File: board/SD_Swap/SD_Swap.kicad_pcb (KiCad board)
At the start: 4 copper layers, 32 x 27 mm, 44 parts, among them J1 USB_C, Q1 Q_Dual_PNP_PNP_E1B1C2E2B2C1, U1 74LVC2G14, U2 RTS5306E, U3 PCB_SD, U4 93AAxxAT, U5 TS3A27518ERTW, U6 SD_SOCKET, U7 AZ1117-3.3, Y1 12MHz

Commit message: tmp
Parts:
- J1: footprint Connector_USB:USB_C_Receptacle_Amphenol_12401548E4-2A -> USB-C:USB_C_Receptacle_Amphenol_10137061-00021LF
- moved J1 5.65 mm to (99.4, 77.9)

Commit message: tmp fix for my mistake
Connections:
- J1 pad A10: /SS_RX- -> unconnected-(J1-RX2--PadA10)
- J1 pad A11: /SS_RX+ -> unconnected-(J1-RX2+-PadA11)
- J1 pad B2: /SS_TX+ -> unconnected-(J1-TX2+-PadB2)
- J1 pad B3: /SS_TX- -> unconnected-(J1-TX2--PadB3)
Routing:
- net /SS_RX+: track 21.2 -> 9.65 mm, vias 2 -> 1
- net /SS_RX-: track 21.1 -> 9.57 mm, vias 2 -> 1
- net /SS_TX+: track 10.3 -> 1.73 mm, vias 1 -> 0
- net /SS_TX-: track 10.2 -> 1.73 mm, vias 1 -> 0

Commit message: tmp
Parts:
- moved C7 1.54 mm to (105.0, 80.6)
- moved C9 0.84 mm to (103.2, 80.7)
- moved R11 0.84 mm to (104.0, 80.7)
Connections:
- D2 pad 2: VCC -> GND
- D2 pad 3: GND -> Net-(D2-A1)
- D2 pad 4: Net-(D2-A1) -> VCC
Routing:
- net +3.3V: track 28.8 -> 26.0 mm, vias 6 -> 5
- net /USB-: track 17.8 -> 15.9 mm
- net /USB+: track 19.0 -> 17.3 mm
- net Net-(U2-REFF): track 2.32 -> 0.80 mm
- net +5V: track 12.5 -> 11.1 mm
- net +1V2: track 23.4 -> 22.7 mm

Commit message: tmp
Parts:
- moved C3 2.48 mm to (116.7, 77.5), turned to 135 degrees
- moved JP3 1.90 mm to (100.3, 93.3)
- moved C2 1.76 mm to (115.7, 78.4), turned to 135 degrees
- moved C7 1.11 mm to (105.5, 81.6), turned to 0 degrees
- moved U5 0.90 mm to (118.9, 81.5)
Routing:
- net +3.3V: track 26.0 -> 32.9 mm
- net Net-(U2-SD_D1): track 13.5 -> 7.67 mm
- net Net-(U5-COM2): track 15.9 -> 10.1 mm
- net /SD_SEL: track 33.7 -> 30.0 mm, vias 2 -> 3
- net Net-(U2-SD_D0): track 12.8 -> 9.40 mm
- net Net-(U5-COM3): track 14.0 -> 10.9 mm
- net Net-(U3-DAT3): track 17.6 -> 15.0 mm
- net Net-(U3-CLK): track 17.6 -> 15.2 mm
- net GND: track 5.56 -> 3.31 mm, vias 87 -> 80
- net Net-(U3-CMD): track 17.6 -> 15.4 mm
- net Net-(U5-COM1): track 13.5 -> 11.4 mm
- net Net-(U2-REFF): track 0.80 -> 2.72 mm
- net Net-(U3-DAT2): track 17.7 -> 15.9 mm
- net Net-(U2-SD_CLK): track 12.9 -> 11.1 mm
- net Net-(U5-COM6): track 14.0 -> 12.5 mm
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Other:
- board text added: "USB3 and 2 are 90ohm diff pair"
- board text added: "{dblquote}(1) Driver Type B Type B driver is the default drive strength, targeted for a fixed impedance distributed system with 50 ohm transmission line, at all available frequencies. Therefore, it is defined as 50 ohm nominal driver. This driver can support total CL of about 15pF for UHS104 card and about 30pF for UHS50 card. Drive strength B is the reference driver for definitions of all the re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"
- board text removed: "UHS50 cards must have 50ohm nominal impedance. There is no length matich requirements but so 0.5mm is ok."

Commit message: tmp
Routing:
- net GND: track 3.31 -> 6.04 mm, vias 80 -> 88
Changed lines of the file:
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@@
     )
     (pad_to_mask_clearance 0.038)
+    (grid_origin 137.7 68.9)
     (pcbplotparams
       (layerselection 0x00000fc_ffffffff)
@@
     (effects (font (size 1 1) (thickness 0.15)) (justify left))
   )
+  (segment (start 119.95 81.15) (end 119.95 81.15) (width 0.25) (layer "F.Cu") (net 1))
+  (segment (start 120.45 81.4) (end 120.2 81.4) (width 0.25) (layer "F.Cu") (net 1))
+  (segment (start 119.95 80.9) (end 119.7 80.9) (width 0.25) (layer "F.Cu") (net 1))
   (segment (start 103.65 92.05) (end 102.625 92.05) (width 0.2) (layer "F.Cu") (net 1))
   (segment (start 102.625 92.05) (end 102.6 92.025) (width 0.2) (layer "F.Cu") (net 1))
-  (segment (start 120.800699 82.313173) (end 119.961009 81.473483) (width 0.25) (layer "F.Cu") (net 1))
-  (segment (start 119.961009 81.473483) (end 118.900349 81.473483) (width 0.25) (layer "F.Cu") (net 1))
+  (segment (start 118.95 81.4) (end 118.900349 81.473483) (width 0.25) (layer "F.Cu") (net 1))
+  (segment (start 119.7 80.9) (end 119.7 80.9) (width 0.25) (layer "F.Cu") (net 1))
+  (segment (start 120.800699 82.313173) (end 120.45 81.962474) (width 0.25) (layer "F.Cu") (net 1))
+  (segment (start 120.2 81.712474) (end 120.45 81.4) (width 0.25) (layer "F.Cu") (net 1))
+  (segment (start 120.2 81.4) (end 119.95 81.4) (width 0.25) (layer "F.Cu") (net 1))
+  (segment (start 119.961009 81.473483) (end 119.95 81.15) (width 0.25) (layer "F.Cu") (net 1))
+  (segment (start 119.95 81.4) (end 119.887526 81.4) (width 0.25) (layer "F.Cu") (net 1))
+  (segment (start 119.887526 81.4) (end 119.961009 81.473483) (width 0.25) (layer "F.Cu") (net 1))
+  (segment (start 120.45 81.962474) (end 120.45 81.65) (width 0.25) (layer "F.Cu") (net 1))
+  (segment (start 119.7 80.9) (end 119.45 80.9) (width 0.25) (layer "F.Cu") (net 1))
+  (segment (start 119.95 81.15) (end 119.95 80.9) (width 0.25) (layer "F.Cu") (net 1))
+  (segment (start 119.95 81.9) (end 120.2 81.712474) (width 0.25) (layer "F.Cu") (net 1))
+  (segment (start 119.45 81.4) (end 118.95 81.4) (width 0.25) (layer "F.Cu") (net 1))
+  (segment (start 120.137526 81.65) (end 119.95 81.9) (width 0.25) (layer "F.Cu") (net 1))
+  (segment (start 119.45 80.9) (end 119.45 81.4) (width 0.25) (layer "F.Cu") (net 1))
+  (segment (start 120.45 81.65) (end 120.137526 81.65) (width 0.25) (layer "F.Cu") (net 1))
   (via (at 93 71) (size 0.6) (drill 0.3) (layers "F.Cu" "B.Cu") (free) (net 1))
+  (via (at 119.95 80.9) (size 0.4) (drill 0.2) (layers "F.Cu" "B.Cu") (net 1))
   (via (at 116 90) (size 0.6) (drill 0.3) (layers "F.Cu" "B.Cu") (free) (net 1))
   (via (at 109 79) (size 0.4) (drill 0.2) (layers "F.Cu" "B.Cu") (net 1))
@@
   (via (at 108.5 77) (size 0.4) (drill 0.2) (layers "F.Cu" "B.Cu") (net 1))
   (via (at 109.5 78.5) (size 0.4) (drill 0.2) (layers "F.Cu" "B.Cu") (net 1))
+  (via (at 118.45 80.4) (size 0.4) (drill 0.2) (layers "F.Cu" "B.Cu") (net 1))
   (via (at 108 78.5) (size 0.4) (drill 0.2) (layers "F.Cu" "B.Cu") (net 1))
   (via (at 108 79.5) (size 0.4) (drill 0.2) (layers "F.Cu" "B.Cu") (net 1))
@@
   (via (at 131 86) (size 0.6) (drill 0.3) (layers "F.Cu" "B.Cu") (free) (net 1))
   (via (at 109 79.5) (size 0.4) (drill 0.2) (layers "F.Cu" "B.Cu") (net 1))
+  (via (at 118.95 80.9) (size 0.4) (drill 0.2) (layers "F.Cu" "B.Cu") (net 1))
   (via (at 109 77) (size 0.4) (drill 0.2) (layers "F.Cu" "B.Cu") (net 1))
   (via (at 107.5 79.5) (size 0.4) (drill 0.2) (layers "F.Cu" "B.Cu") (net 1))
@@
   (via (at 94 93) (size 0.6) (drill 0.3) (layers "F.Cu" "B.Cu") (free) (net 1))
   (via (at 109.5 79.5) (size 0.4) (drill 0.2) (layers "F.Cu" "B.Cu") (net 1))
+  (via (at 119.95 81.9) (size 0.4) (drill 0.2) (layers "F.Cu" "B.Cu") (net 1))
   (via (at 115 71) (size 0.6) (drill 0.3) (layers "F.Cu" "B.Cu") (free) (net 1))
   (via (at 120 86) (size 0.6) (drill 0.3) (layers "F.Cu" "B.Cu") (free) (net 1))
@@
   (via (at 94 70) (size 0.6) (drill 0.3) (layers "F.Cu" "B.Cu") (free) (net 1))
   (via (at 107.5 78.5) (size 0.4) (drill 0.2) (layers "F.Cu" "B.Cu") (net 1))
+  (via (at 119.45 81.4) (size 0.4) (drill 0.2) (layers "F.Cu" "B.Cu") (net 1))
   (via (at 96 94) (size 0.6) (drill 0.3) (layers "F.Cu" "B.Cu") (free) (net 1))
   (via (at 107 78) (size 0.4) (drill 0.2) (layers "F.Cu" "B.Cu") (net 1))
   (via (at 109.6 94) (size 0.6) (drill 0.3) (layers "F.Cu" "B.Cu") (free) (net 1))
+  (via (at 120.45 81.4) (size 0.4) (drill 0.2) (layers "F.Cu" "B.Cu") (net 1))
+  (via (at 119.45 80.4) (size 0.4) (drill 0.2) (layers "F.Cu" "B.Cu") (net 1))
   (via (at 108.5 79) (size 0.4) (drill 0.2) (layers "F.Cu" "B.Cu") (net 1))
   (via (at 108 77) (size 0.4) (drill 0.2) (layers "F.Cu" "B.Cu") (net 1))
@@
   (via (at 109.5 78) (size 0.4) (drill 0.2) (layers "F.Cu" "B.Cu") (net 1))
   (via (at 110 77) (size 0.4) (drill 0.2) (layers "F.Cu" "B.Cu") (net 1))
+  (via (at 118.95 79.9) (size 0.4) (drill 0.2) (layers "F.Cu" "B.Cu") (net 1))
   (via (at 110 79) (size 0.4) (drill 0.2) (layers "F.Cu" "B.Cu") (net 1))
   (via (at 108.5 78.5) (size 0.4) (drill 0.2) (layers "F.Cu" "B.Cu") (net 1))
@@
   (via (at 114.2 86.4) (size 0.4) (drill 0.2) (layers "F.Cu" "B.Cu") (net 48))
   (via (at 118.096015 78.671573) (size 0.4) (drill 0.2) (layers "F.Cu" "B.Cu") (net 48))
-  (segment (start 118.096015 78.671573) (end 118.096015 83.303985) (width 0.22) (layer "In1.Cu") (net 48))
+  (segment (start 117.85 78.917588) (end 118.096015 78.671573) (width 0.22) (layer "In1.Cu") (net 48))
+  (segment (start 117.85 83.55) (end 115 86.4) (width 0.22) (layer "In1.Cu") (net 48))
   (segment (start 115 86.4) (end 114.2 86.4) (width 0.22) (layer "In1.Cu") (net 48))
-  (segment (start 118.096015 83.303985) (end 115 86.4) (width 0.22) (layer "In1.Cu") (net 48))
+  (segment (start 117.85 83.55) (end 117.85 78.917588) (width 0.22) (layer "In1.Cu") (net 48))
   (segment (start 114.15 87.311715) (end 114.15 86.45) (width 0.22) (layer "B.Cu") (net 48))
   (segment (start 114.15 86.45) (end 114.2 86.4) (width 0.22) (layer "B.Cu") (net 48))
@@
   )
   (zone (net 3) (net_name "+3.3V") (layer "In1.Cu") (hatch edge 0.508)
-    (connect_pads (clearance 0.2))
+    (connect_pads (clearance 0.3))
     (min_thickness 0.15) (filled_areas_thickness no)
     (fill yes (thermal_gap 0.1) (thermal_bridge_width 0.2))
@@
   )
   (zone (net 10) (net_name "/SD_VCC") (layer "In2.Cu") (hatch edge 0.508)
-    (connect_pads (clearance 0.2))
+    (connect_pads (clearance 0.3))
     (min_thickness 0.15) (filled_areas_thickness no)
     (fill yes (thermal_gap 0.1) (thermal_bridge_width 0.2))

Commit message: final?
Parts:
- moved C5 1.67 mm to (111.7, 82.6)
- moved C4 1.59 mm to (111.7, 81.8)
- moved U7 0.60 mm to (106.6, 85.7)
- moved C1 0.35 mm to (113.8, 91.7)
- moved Q1 0.35 mm to (111.6, 91.3)
- moved R5 0.25 mm to (105.3, 90.2)
- moved R7 0.25 mm to (107.1, 90.2)
- moved R8 0.10 mm to (111.3, 93.7)
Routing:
- net /USB+: track 17.3 -> 15.9 mm
- net /USB-: track 15.9 -> 14.7 mm
- net +3.3V: track 32.9 -> 33.7 mm
- net Net-(Q1B-B2): track 6.31 -> 5.77 mm

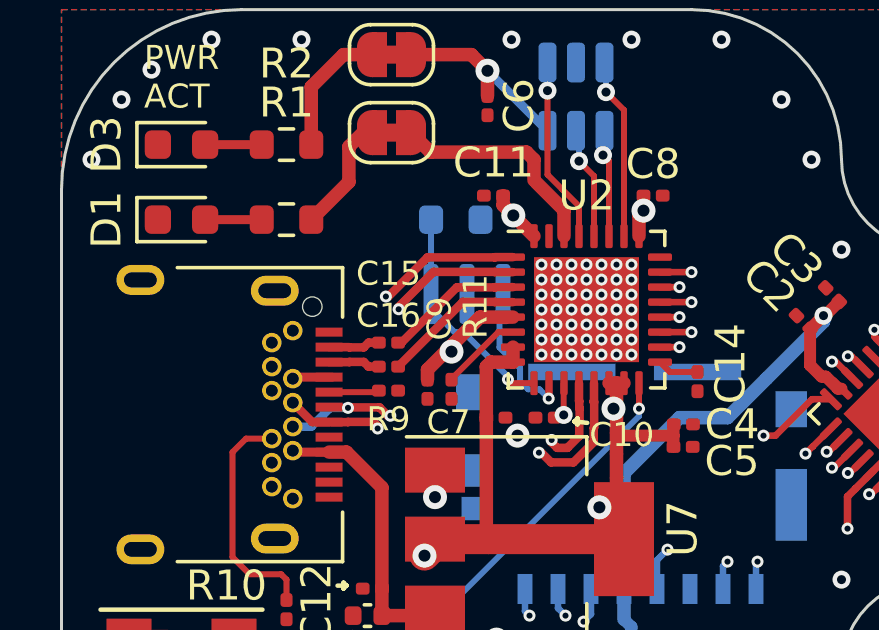
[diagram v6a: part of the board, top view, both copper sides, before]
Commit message: fix usbc
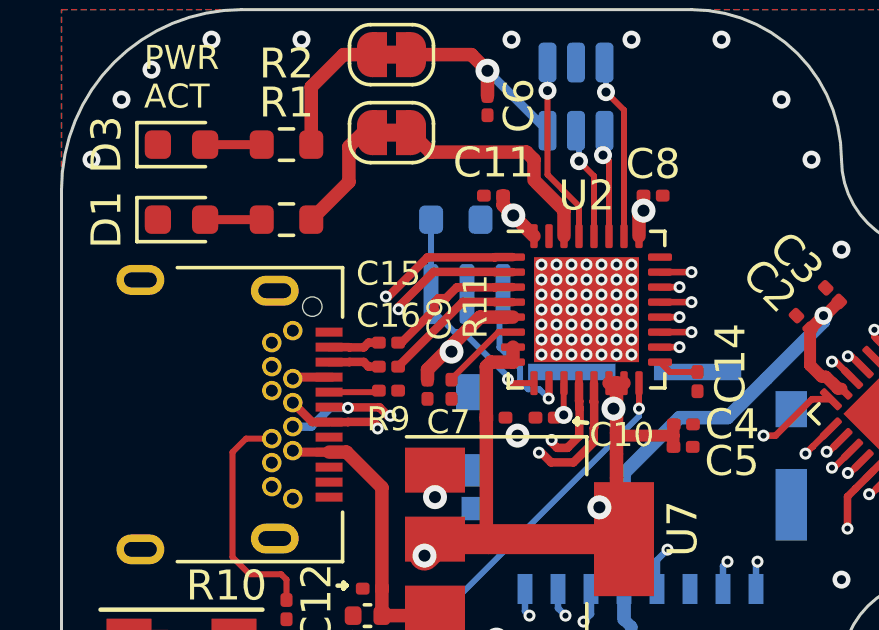
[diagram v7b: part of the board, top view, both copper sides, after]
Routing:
- net /USB-: track 14.7 -> 15.9 mm
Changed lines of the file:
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@@
   (via (at 107.337809 82.34378) (size 0.4) (drill 0.2) (layers "F.Cu" "B.Cu") (net 21))
   (segment (start 107.337809 82.34378) (end 107.337809 82.425806) (width 0.284) (layer "In2.Cu") (net 21))
-  (segment (start 107.174442 83.882191) (end 105.206277 83.882191) (width 0.1902) (layer "In2.Cu") (net 21))
-  (segment (start 107.5951 83.461533) (end 107.174442 83.882191) (width 0.1902) (layer "In2.Cu") (net 21))
-  (segment (start 101.686219 81.962133) (end 101.537867 81.962133) (width 0.1902) (layer "In2.Cu") (net 21))
-  (segment (start 102.319186 82.5951) (end 101.686219 81.962133) (width 0.1902) (layer "In2.Cu") (net 21))
-  (segment (start 103.919186 82.5951) (end 102.319186 82.5951) (width 0.1902) (layer "In2.Cu") (net 21))
-  (segment (start 107.337809 82.34378) (end 107.337809 82.492132) (width 0.1902) (layer "In2.Cu") (net 21))
-  (segment (start 107.5951 82.749423) (end 107.5951 83.461533) (width 0.1902) (layer "In2.Cu") (net 21))
-  (segment (start 107.337809 82.492132) (end 107.5951 82.749423) (width 0.1902) (layer "In2.Cu") (net 21))
-  (segment (start 105.206277 83.882191) (end 103.919186 82.5951) (width 0.1902) (layer "In2.Cu") (net 21))
+  (segment (start 105.761547 84.437462) (end 105.806277 84.437462) (width 0.1902) (layer "In2.Cu") (net 21))
+  (segment (start 103.76 82.5951) (end 103.919186 82.5951) (width 0.1902) (layer "In2.Cu") (net 21))
+  (segment (start 103.437625 82.872726) (end 103.437625 82.872725) (width 0.1902) (layer "In2.Cu") (net 21))
+  (segment (start 103.71525 82.5951) (end 103.76 82.5951) (width 0.1902) (layer "In2.Cu") (net 21))
+  (segment (start 107.5951 83.461533) (end 107.5951 82.749423) (width 0.1902) (layer "In2.Cu") (net 21))
+  (segment (start 101.537867 81.962133) (end 101.686219 81.962133) (width 0.1902) (layer "In2.Cu") (net 21))
+  (segment (start 107.5951 82.749423) (end 107.337809 82.492132) (width 0.1902) (layer "In2.Cu") (net 21))
+  (segment (start 103.11525 83.150351) (end 103.16 83.150351) (width 0.1902) (layer "In2.Cu") (net 21))
+  (segment (start 101.686219 81.962133) (end 102.319186 82.5951) (width 0.1902) (layer "In2.Cu") (net 21))
+  (segment (start 106.083912 84.159827) (end 106.083912 84.159826) (width 0.1902) (layer "In2.Cu") (net 21))
+  (segment (start 102.837625 82.872725) (end 102.837625 82.872726) (width 0.1902) (layer "In2.Cu") (net 21))
+  (segment (start 106.361547 83.882191) (end 106.406277 83.882191) (width 0.1902) (layer "In2.Cu") (net 21))
+  (segment (start 107.174442 83.882191) (end 107.5951 83.461533) (width 0.1902) (layer "In2.Cu") (net 21))
+  (segment (start 107.337809 82.492132) (end 107.337809 82.34378) (width 0.1902) (layer "In2.Cu") (net 21))
+  (segment (start 106.406277 83.882191) (end 107.174442 83.882191) (width 0.1902) (layer "In2.Cu") (net 21))
+  (segment (start 102.319186 82.5951) (end 102.56 82.5951) (width 0.1902) (layer "In2.Cu") (net 21))
+  (segment (start 105.483912 84.159826) (end 105.483912 84.159827) (width 0.1902) (layer "In2.Cu") (net 21))
+  (segment (start 103.919186 82.5951) (end 105.206277 83.882191) (width 0.1902) (layer "In2.Cu") (net 21))
+  (arc (start 105.206277 83.882191) (mid 105.402595 83.963508) (end 105.483912 84.159826) (width 0.1902) (layer "In2.Cu") (net 21))
+  (arc (start 105.806277 84.437462) (mid 106.002595 84.356145) (end 106.083912 84.159827) (width 0.1902) (layer "In2.Cu") (net 21))
+  (arc (start 102.56 82.5951) (mid 102.756311 82.676414) (end 102.837625 82.872725) (width 0.1902) (layer "In2.Cu") (net 21))
+  (arc (start 103.16 83.150351) (mid 103.356311 83.069037) (end 103.437625 82.872726) (width 0.1902) (layer "In2.Cu") (net 21))
+  (arc (start 105.483912 84.159827) (mid 105.565229 84.356145) (end 105.761547 84.437462) (width 0.1902) (layer "In2.Cu") (net 21))
+  (arc (start 106.083912 84.159826) (mid 106.165229 83.963508) (end 106.361547 83.882191) (width 0.1902) (layer "In2.Cu") (net 21))
+  (arc (start 103.437625 82.872725) (mid 103.518939 82.676414) (end 103.71525 82.5951) (width 0.1902) (layer "In2.Cu") (net 21))
+  (arc (start 102.837625 82.872726) (mid 102.918939 83.069037) (end 103.11525 83.150351) (width 0.1902) (layer "In2.Cu") (net 21))
   (segment (start 108.755313 81.931501) (end 108.742 81.944813) (width 0.284) (layer "F.Cu") (net 22))
   (segment (start 108.065611 83.092) (end 107.319523 83.092) (width 0.284) (layer "F.Cu") (net 22))
@@
   (segment (start 113.05 86.55) (end 113.2 86.4) (width 0.22) (layer "B.Cu") (net 49))
   (segment (start 113.05 87.311715) (end 113.05 86.55) (width 0.22) (layer "B.Cu") (net 49))
-  (segment (start 104.17752 77.258) (end 102.33552 79.1) (width 0.284) (layer "F.Cu") (net 50))
+  (segment (start 105.441999 77.258) (end 104.17752 77.258) (width 0.284) (layer "F.Cu") (net 50))
+  (segment (start 105.449999 77.25) (end 105.441999 77.258) (width 0.284) (layer "F.Cu") (net 50))
+  (segment (start 103.430347 77.759263) (end 103.430347 78.005169) (width 0.284) (layer "F.Cu") (net 50))
   (segment (start 106.05 77.25) (end 105.449999 77.25) (width 0.284) (layer "F.Cu") (net 50))
+  (segment (start 103.430347 78.005169) (end 103.215821 78.219699) (width 0.284) (layer "F.Cu") (net 50))
+  (segment (start 103.571852 77.617759) (end 103.430347 77.759263) (width 0.284) (layer "F.Cu") (net 50))
   (segment (start 102.33552 79.1) (end 102.22 79.1) (width 0.284) (layer "F.Cu") (net 50))
-  (segment (start 105.449999 77.25) (end 105.441999 77.258) (width 0.284) (layer "F.Cu") (net 50))
-  (segment (start 105.441999 77.258) (end 104.17752 77.258) (width 0.284) (layer "F.Cu") (net 50))
+  (segment (start 103.215821 78.219699) (end 102.33552 79.1) (width 0.284) (layer "F.Cu") (net 50))
+  (segment (start 103.81776 77.61776) (end 103.571852 77.617759) (width 0.284) (layer "F.Cu") (net 50))
+  (segment (start 104.17752 77.258) (end 103.81776 77.61776) (width 0.284) (layer "F.Cu") (net 50))
   (segment (start 105.441999 77.742) (end 105.449999 77.75) (width 0.284) (layer "F.Cu") (net 51))
   (segment (start 105.449999 77.75) (end 106.05 77.75) (width 0.284) (layer "F.Cu") (net 51))
@@
         (xy 105.811362 81.5)
         (xy 108.511362 81.5)
-        (xy 108.5 83.4)
-        (xy 107.7 84.4)
-        (xy 104.7 84.4)
-        (xy 103.7 83.4)
+        (xy 108.5 83.9)
+        (xy 107.7 84.9)
+        (xy 104.95 84.9)
+        (xy 103.45 83.4)
         (xy 99.4 83.4)
         (xy 100.2 82.6)
